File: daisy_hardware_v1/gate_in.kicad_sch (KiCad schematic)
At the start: 5 parts, among them J6 PJ398SM-12, Q1 MMBT3904

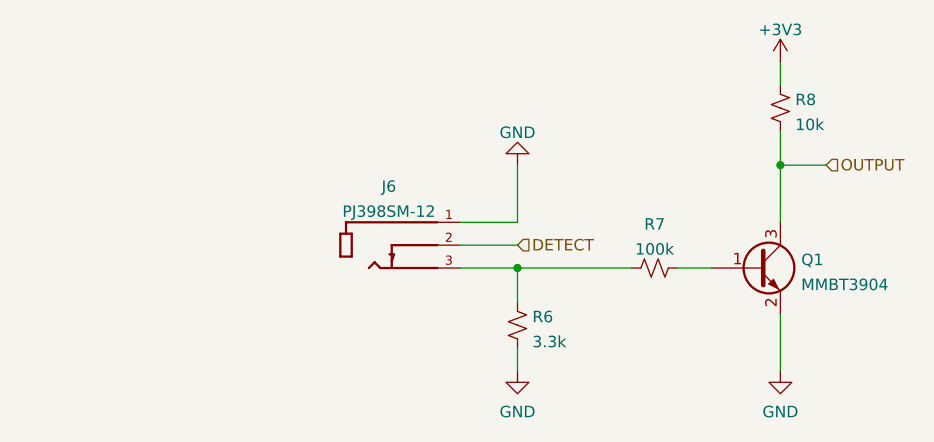
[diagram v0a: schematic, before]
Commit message: first pass of daisy schematic
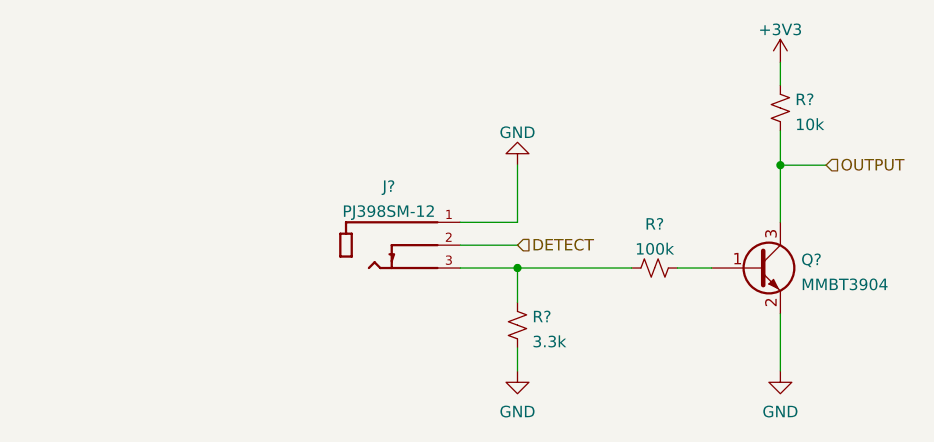
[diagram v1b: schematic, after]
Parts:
- renumbered J6 to J?, Q1 to Q?, R8 to R?, R7 to R?, R6 to R?
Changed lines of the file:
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@@
   (symbol (lib_id "Device:R_Small_US") (at 121.92 91.44 180)
     (in_bom yes) (on_board yes) (fields_autoplaced)
-    (property "Reference" "R8" (id 0) (at 123.571 90.5315 0)
+    (property "Reference" "R?" (id 0) (at 123.571 90.5315 0)
       (effects (font (size 1.27 1.27)) (justify right))
     )
@@
   (symbol (lib_id "power:GND") (at 121.92 120.65 0)
     (in_bom yes) (on_board yes) (fields_autoplaced)
-    (property "Reference" "#PWR0137" (id 0) (at 121.92 127 0)
+    (property "Reference" "#PWR?" (id 0) (at 121.92 127 0)
       (effects (font (size 1.27 1.27)) hide)
     )
@@
   (symbol (lib_id "power:GND") (at 92.71 120.65 0)
     (in_bom yes) (on_board yes) (fields_autoplaced)
-    (property "Reference" "#PWR0138" (id 0) (at 92.71 127 0)
+    (property "Reference" "#PWR?" (id 0) (at 92.71 127 0)
       (effects (font (size 1.27 1.27)) hide)
     )
@@
   (symbol (lib_id "PJ398SM-12:PJ398SM-12") (at 78.74 104.14 0)
     (in_bom yes) (on_board yes) (fields_autoplaced)
-    (property "Reference" "J6" (id 0) (at 78.4225 100.1735 0))
+    (property "Reference" "J?" (id 0) (at 78.4225 100.1735 0))
     (property "Value" "PJ398SM-12" (id 1) (at 78.4225 102.9486 0))
     (property "Footprint" "THONK_PJ398SM-12" (id 2) (at 78.74 104.14 0)
@@
   (symbol (lib_id "power:GND") (at 92.71 97.79 180)
     (in_bom yes) (on_board yes) (fields_autoplaced)
-    (property "Reference" "#PWR0136" (id 0) (at 92.71 91.44 0)
+    (property "Reference" "#PWR?" (id 0) (at 92.71 91.44 0)
       (effects (font (size 1.27 1.27)) hide)
     )
@@
   (symbol (lib_id "Device:R_Small_US") (at 107.95 109.22 90)
     (in_bom yes) (on_board yes) (fields_autoplaced)
-    (property "Reference" "R7" (id 0) (at 107.95 104.3645 90))
+    (property "Reference" "R?" (id 0) (at 107.95 104.3645 90))
     (property "Value" "100k" (id 1) (at 107.95 107.1396 90))
     (property "Footprint" "" (id 2) (at 107.95 109.22 0)
@@
   (symbol (lib_id "Transistor_BJT:MMBT3904") (at 119.38 109.22 0)
     (in_bom yes) (on_board yes) (fields_autoplaced)
-    (property "Reference" "Q1" (id 0) (at 124.2314 108.3115 0)
+    (property "Reference" "Q?" (id 0) (at 124.2314 108.3115 0)
       (effects (font (size 1.27 1.27)) (justify left))
     )
@@
   (symbol (lib_id "power:+3V3") (at 121.92 86.36 0)
     (in_bom yes) (on_board yes) (fields_autoplaced)
-    (property "Reference" "#PWR0139" (id 0) (at 121.92 90.17 0)
+    (property "Reference" "#PWR?" (id 0) (at 121.92 90.17 0)
       (effects (font (size 1.27 1.27)) hide)
     )
@@
   (symbol (lib_id "Device:R_Small_US") (at 92.71 115.57 0)
     (in_bom yes) (on_board yes) (fields_autoplaced)
-    (property "Reference" "R6" (id 0) (at 94.361 114.6615 0)
+    (property "Reference" "R?" (id 0) (at 94.361 114.6615 0)
       (effects (font (size 1.27 1.27)) (justify left))
     )

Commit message: Schematics coming along
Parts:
- J7: renamed from J?; footprint THONK_PJ398SM-12 -> Connector_Audio:Jack_3.5mm_QingPu_WQP-PJ398SM_Vertical_CircularHoles
- gave numbers to parts that had none: 4
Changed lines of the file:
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@@
   (symbol (lib_id "Device:R_Small_US") (at 121.92 91.44 180)
     (in_bom yes) (on_board yes) (fields_autoplaced)
-    (property "Reference" "R?" (id 0) (at 123.571 90.5315 0)
+    (property "Reference" "R11" (id 0) (at 123.571 90.5315 0)
       (effects (font (size 1.27 1.27)) (justify right))
     )
@@
   (symbol (lib_id "power:GND") (at 121.92 120.65 0)
     (in_bom yes) (on_board yes) (fields_autoplaced)
-    (property "Reference" "#PWR?" (id 0) (at 121.92 127 0)
+    (property "Reference" "#PWR0141" (id 0) (at 121.92 127 0)
       (effects (font (size 1.27 1.27)) hide)
     )
@@
   (symbol (lib_id "power:GND") (at 92.71 120.65 0)
     (in_bom yes) (on_board yes) (fields_autoplaced)
-    (property "Reference" "#PWR?" (id 0) (at 92.71 127 0)
+    (property "Reference" "#PWR0142" (id 0) (at 92.71 127 0)
       (effects (font (size 1.27 1.27)) hide)
     )
@@
   (symbol (lib_id "PJ398SM-12:PJ398SM-12") (at 78.74 104.14 0)
     (in_bom yes) (on_board yes) (fields_autoplaced)
-    (property "Reference" "J?" (id 0) (at 78.4225 100.1735 0))
+    (property "Reference" "J7" (id 0) (at 78.4225 100.1735 0))
     (property "Value" "PJ398SM-12" (id 1) (at 78.4225 102.9486 0))
-    (property "Footprint" "THONK_PJ398SM-12" (id 2) (at 78.74 104.14 0)
+    (property "Footprint" "Connector_Audio:Jack_3.5mm_QingPu_WQP-PJ398SM_Vertical_CircularHoles" (id 2) (at 78.74 104.14 0)
       (effects (font (size 1.27 1.27)) (justify left bottom) hide)
     )
@@
   (symbol (lib_id "power:GND") (at 92.71 97.79 180)
     (in_bom yes) (on_board yes) (fields_autoplaced)
-    (property "Reference" "#PWR?" (id 0) (at 92.71 91.44 0)
+    (property "Reference" "#PWR0140" (id 0) (at 92.71 91.44 0)
       (effects (font (size 1.27 1.27)) hide)
     )
@@
   (symbol (lib_id "Device:R_Small_US") (at 107.95 109.22 90)
     (in_bom yes) (on_board yes) (fields_autoplaced)
-    (property "Reference" "R?" (id 0) (at 107.95 104.3645 90))
+    (property "Reference" "R10" (id 0) (at 107.95 104.3645 90))
     (property "Value" "100k" (id 1) (at 107.95 107.1396 90))
     (property "Footprint" "" (id 2) (at 107.95 109.22 0)
@@
   (symbol (lib_id "Transistor_BJT:MMBT3904") (at 119.38 109.22 0)
     (in_bom yes) (on_board yes) (fields_autoplaced)
-    (property "Reference" "Q?" (id 0) (at 124.2314 108.3115 0)
+    (property "Reference" "Q2" (id 0) (at 124.2314 108.3115 0)
       (effects (font (size 1.27 1.27)) (justify left))
     )
@@
   (symbol (lib_id "power:+3V3") (at 121.92 86.36 0)
     (in_bom yes) (on_board yes) (fields_autoplaced)
-    (property "Reference" "#PWR?" (id 0) (at 121.92 90.17 0)
+    (property "Reference" "#PWR0143" (id 0) (at 121.92 90.17 0)
       (effects (font (size 1.27 1.27)) hide)
     )
@@
   (symbol (lib_id "Device:R_Small_US") (at 92.71 115.57 0)
     (in_bom yes) (on_board yes) (fields_autoplaced)
-    (property "Reference" "R?" (id 0) (at 94.361 114.6615 0)
+    (property "Reference" "R9" (id 0) (at 94.361 114.6615 0)
       (effects (font (size 1.27 1.27)) (justify left))
     )

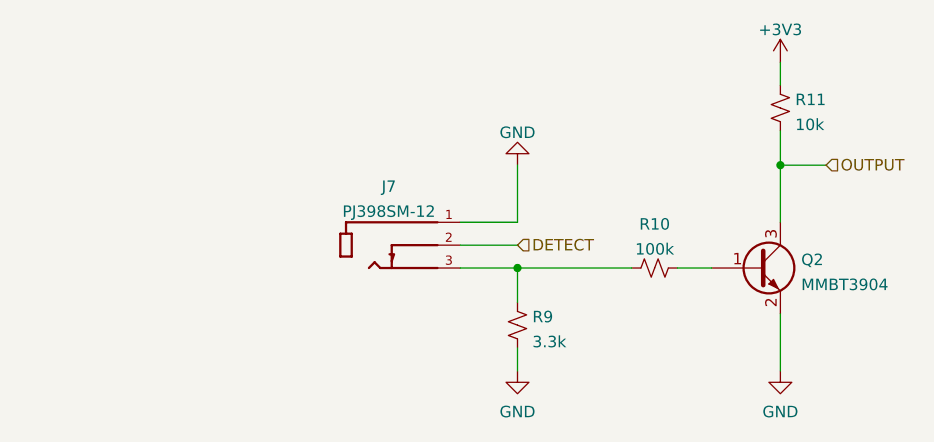
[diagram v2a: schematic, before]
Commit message: Update power + add start/end to schematics
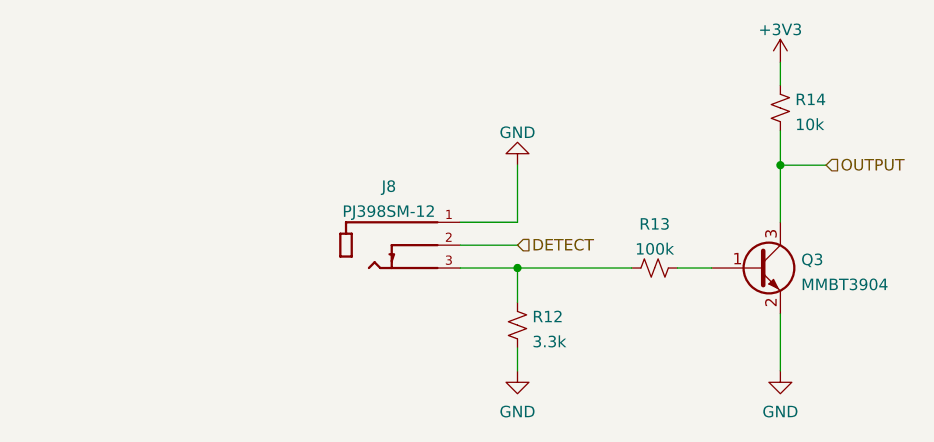
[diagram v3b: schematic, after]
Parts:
- J8: renamed from J7; footprint Connector_Audio:Jack_3.5mm_QingPu_WQP-PJ398SM_Vertical_CircularHoles -> lowstepper_internal_footprint_lib:THONK_PJ398SM-12
- renumbered Q2 to Q3, R9 to R12, R10 to R13, R11 to R14
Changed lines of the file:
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@@
   (symbol (lib_id "Device:R_Small_US") (at 121.92 91.44 180)
     (in_bom yes) (on_board yes) (fields_autoplaced)
-    (property "Reference" "R11" (id 0) (at 123.571 90.5315 0)
+    (property "Reference" "R14" (id 0) (at 123.571 90.5315 0)
       (effects (font (size 1.27 1.27)) (justify right))
     )
@@
   (symbol (lib_id "power:GND") (at 121.92 120.65 0)
     (in_bom yes) (on_board yes) (fields_autoplaced)
-    (property "Reference" "#PWR0141" (id 0) (at 121.92 127 0)
+    (property "Reference" "#PWR0157" (id 0) (at 121.92 127 0)
       (effects (font (size 1.27 1.27)) hide)
     )
@@
   (symbol (lib_id "power:GND") (at 92.71 120.65 0)
     (in_bom yes) (on_board yes) (fields_autoplaced)
-    (property "Reference" "#PWR0142" (id 0) (at 92.71 127 0)
+    (property "Reference" "#PWR0158" (id 0) (at 92.71 127 0)
       (effects (font (size 1.27 1.27)) hide)
     )
@@
   (symbol (lib_id "PJ398SM-12:PJ398SM-12") (at 78.74 104.14 0)
     (in_bom yes) (on_board yes) (fields_autoplaced)
-    (property "Reference" "J7" (id 0) (at 78.4225 100.1735 0))
+    (property "Reference" "J8" (id 0) (at 78.4225 100.1735 0))
     (property "Value" "PJ398SM-12" (id 1) (at 78.4225 102.9486 0))
-    (property "Footprint" "Connector_Audio:Jack_3.5mm_QingPu_WQP-PJ398SM_Vertical_CircularHoles" (id 2) (at 78.74 104.14 0)
+    (property "Footprint" "lowstepper_internal_footprint_lib:THONK_PJ398SM-12" (id 2) (at 78.74 104.14 0)
       (effects (font (size 1.27 1.27)) (justify left bottom) hide)
     )
@@
   (symbol (lib_id "power:GND") (at 92.71 97.79 180)
     (in_bom yes) (on_board yes) (fields_autoplaced)
-    (property "Reference" "#PWR0140" (id 0) (at 92.71 91.44 0)
+    (property "Reference" "#PWR0156" (id 0) (at 92.71 91.44 0)
       (effects (font (size 1.27 1.27)) hide)
     )
@@
   (symbol (lib_id "Device:R_Small_US") (at 107.95 109.22 90)
     (in_bom yes) (on_board yes) (fields_autoplaced)
-    (property "Reference" "R10" (id 0) (at 107.95 104.3645 90))
+    (property "Reference" "R13" (id 0) (at 107.95 104.3645 90))
     (property "Value" "100k" (id 1) (at 107.95 107.1396 90))
     (property "Footprint" "" (id 2) (at 107.95 109.22 0)
@@
   (symbol (lib_id "Transistor_BJT:MMBT3904") (at 119.38 109.22 0)
     (in_bom yes) (on_board yes) (fields_autoplaced)
-    (property "Reference" "Q2" (id 0) (at 124.2314 108.3115 0)
+    (property "Reference" "Q3" (id 0) (at 124.2314 108.3115 0)
       (effects (font (size 1.27 1.27)) (justify left))
     )
@@
   (symbol (lib_id "power:+3V3") (at 121.92 86.36 0)
     (in_bom yes) (on_board yes) (fields_autoplaced)
-    (property "Reference" "#PWR0143" (id 0) (at 121.92 90.17 0)
+    (property "Reference" "#PWR0159" (id 0) (at 121.92 90.17 0)
       (effects (font (size 1.27 1.27)) hide)
     )
@@
   (symbol (lib_id "Device:R_Small_US") (at 92.71 115.57 0)
     (in_bom yes) (on_board yes) (fields_autoplaced)
-    (property "Reference" "R9" (id 0) (at 94.361 114.6615 0)
+    (property "Reference" "R12" (id 0) (at 94.361 114.6615 0)
       (effects (font (size 1.27 1.27)) (justify left))
     )

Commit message: Start splitting up board
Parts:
- R10: renamed from R13; footprint (none) -> Resistor_SMD:R_0603_1608Metric
- R11: renamed from R14; footprint (none) -> Resistor_SMD:R_0603_1608Metric
- R9: renamed from R12; footprint (none) -> Resistor_SMD:R_0603_1608Metric
- renumbered J8 to J7, Q3 to Q2
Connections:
- net INPUT_BOTTOM: now reaches R10.1, R9.1
- net INPUT_BOTTOM: no longer J7.3
- new net INPUT_TOP: J7.3
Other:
- moved on the sheet: J7
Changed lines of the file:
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@@
     (stroke (width 0) (type default) (color 0 0 0 0))
   )
-  (wire (pts (xy 86.36 104.14) (xy 92.71 104.14))
+  (wire (pts (xy 52.07 104.14) (xy 92.71 104.14))
     (stroke (width 0) (type default) (color 0 0 0 0))
   )
   (wire (pts (xy 86.36 109.22) (xy 92.71 109.22))
+    (stroke (width 0) (type default) (color 0 0 0 0))
+  )
+  (wire (pts (xy 52.07 109.22) (xy 54.61 109.22))
     (stroke (width 0) (type default) (color 0 0 0 0))
   )
@@
     (stroke (width 0) (type default) (color 0 0 0 0))
   )
-  (wire (pts (xy 86.36 106.68) (xy 92.71 106.68))
+  (wire (pts (xy 52.07 106.68) (xy 92.71 106.68))
     (stroke (width 0) (type default) (color 0 0 0 0))
   )
   (wire (pts (xy 121.92 114.3) (xy 121.92 120.65))
     (stroke (width 0) (type default) (color 0 0 0 0))
+  )
+  (hierarchical_label "INPUT_BOTTOM" (shape input) (at 86.36 109.22 180)
+    (effects (font (size 1.27 1.27)) (justify right))
+  )
+  (hierarchical_label "INPUT_TOP" (shape input) (at 54.61 109.22 0)
+    (effects (font (size 1.27 1.27)) (justify left))
   )
   (hierarchical_label "DETECT" (shape input) (at 92.71 106.68 0)
@@
   (symbol (lib_id "Device:R_Small_US") (at 121.92 91.44 180)
     (in_bom yes) (on_board yes) (fields_autoplaced)
-    (property "Reference" "R14" (id 0) (at 123.571 90.5315 0)
+    (property "Reference" "R11" (id 0) (at 123.571 90.5315 0)
       (effects (font (size 1.27 1.27)) (justify right))
     )
@@
       (effects (font (size 1.27 1.27)) (justify right))
     )
-    (property "Footprint" "" (id 2) (at 121.92 91.44 0)
+    (property "Footprint" "Resistor_SMD:R_0603_1608Metric" (id 2) (at 121.92 91.44 0)
       (effects (font (size 1.27 1.27)) hide)
     )
@@
   (symbol (lib_id "power:GND") (at 121.92 120.65 0)
     (in_bom yes) (on_board yes) (fields_autoplaced)
-    (property "Reference" "#PWR0157" (id 0) (at 121.92 127 0)
+    (property "Reference" "#PWR0141" (id 0) (at 121.92 127 0)
       (effects (font (size 1.27 1.27)) hide)
     )
@@
   (symbol (lib_id "power:GND") (at 92.71 120.65 0)
     (in_bom yes) (on_board yes) (fields_autoplaced)
-    (property "Reference" "#PWR0158" (id 0) (at 92.71 127 0)
+    (property "Reference" "#PWR0142" (id 0) (at 92.71 127 0)
       (effects (font (size 1.27 1.27)) hide)
     )
@@
     (pin "1")
   )
-  (symbol (lib_id "PJ398SM-12:PJ398SM-12") (at 78.74 104.14 0)
+  (symbol (lib_id "PJ398SM-12:PJ398SM-12") (at 44.45 104.14 0)
     (in_bom yes) (on_board yes) (fields_autoplaced)
-    (property "Reference" "J8" (id 0) (at 78.4225 100.1735 0))
-    (property "Value" "PJ398SM-12" (id 1) (at 78.4225 102.9486 0))
-    (property "Footprint" "lowstepper_internal_footprint_lib:THONK_PJ398SM-12" (id 2) (at 78.74 104.14 0)
+    (property "Reference" "J7" (id 0) (at 44.1325 100.1735 0))
+    (property "Value" "PJ398SM-12" (id 1) (at 44.1325 102.9486 0))
+    (property "Footprint" "lowstepper_internal_footprint_lib:THONK_PJ398SM-12" (id 2) (at 44.45 104.14 0)
       (effects (font (size 1.27 1.27)) (justify left bottom) hide)
     )
-    (property "Datasheet" "" (id 3) (at 78.74 104.14 0)
+    (property "Datasheet" "" (id 3) (at 44.45 104.14 0)
       (effects (font (size 1.27 1.27)) (justify left bottom) hide)
     )
-    (property "MAXIMUM_PACKAGE_HEIGHT" "14.5 mm" (id 4) (at 78.74 104.14 0)
+    (property "MAXIMUM_PACKAGE_HEIGHT" "14.5 mm" (id 4) (at 44.45 104.14 0)
       (effects (font (size 1.27 1.27)) (justify left bottom) hide)
     )
-    (property "MANUFACTURER" "Thonk" (id 5) (at 78.74 104.14 0)
+    (property "MANUFACTURER" "Thonk" (id 5) (at 44.45 104.14 0)
       (effects (font (size 1.27 1.27)) (justify left bottom) hide)
     )
-    (property "PARTREV" "1" (id 6) (at 78.74 104.14 0)
+    (property "PARTREV" "1" (id 6) (at 44.45 104.14 0)
       (effects (font (size 1.27 1.27)) (justify left bottom) hide)
     )
-    (property "STANDARD" "Manufacturer Recommendations" (id 7) (at 78.74 104.14 0)
+    (property "STANDARD" "Manufacturer Recommendations" (id 7) (at 44.45 104.14 0)
       (effects (font (size 1.27 1.27)) (justify left bottom) hide)
     )
@@
   (symbol (lib_id "power:GND") (at 92.71 97.79 180)
     (in_bom yes) (on_board yes) (fields_autoplaced)
-    (property "Reference" "#PWR0156" (id 0) (at 92.71 91.44 0)
+    (property "Reference" "#PWR0140" (id 0) (at 92.71 91.44 0)
       (effects (font (size 1.27 1.27)) hide)
     )
@@
   (symbol (lib_id "Device:R_Small_US") (at 107.95 109.22 90)
     (in_bom yes) (on_board yes) (fields_autoplaced)
-    (property "Reference" "R13" (id 0) (at 107.95 104.3645 90))
+    (property "Reference" "R10" (id 0) (at 107.95 104.3645 90))
     (property "Value" "100k" (id 1) (at 107.95 107.1396 90))
-    (property "Footprint" "" (id 2) (at 107.95 109.22 0)
+    (property "Footprint" "Resistor_SMD:R_0603_1608Metric" (id 2) (at 107.95 109.22 0)
       (effects (font (size 1.27 1.27)) hide)
     )
@@
   (symbol (lib_id "Transistor_BJT:MMBT3904") (at 119.38 109.22 0)
     (in_bom yes) (on_board yes) (fields_autoplaced)
-    (property "Reference" "Q3" (id 0) (at 124.2314 108.3115 0)
+    (property "Reference" "Q2" (id 0) (at 124.2314 108.3115 0)
       (effects (font (size 1.27 1.27)) (justify left))
     )
@@
   (symbol (lib_id "power:+3V3") (at 121.92 86.36 0)
     (in_bom yes) (on_board yes) (fields_autoplaced)
-    (property "Reference" "#PWR0159" (id 0) (at 121.92 90.17 0)
+    (property "Reference" "#PWR0143" (id 0) (at 121.92 90.17 0)
       (effects (font (size 1.27 1.27)) hide)
     )
@@
   (symbol (lib_id "Device:R_Small_US") (at 92.71 115.57 0)
     (in_bom yes) (on_board yes) (fields_autoplaced)
-    (property "Reference" "R12" (id 0) (at 94.361 114.6615 0)
+    (property "Reference" "R9" (id 0) (at 94.361 114.6615 0)
       (effects (font (size 1.27 1.27)) (justify left))
     )
@@
       (effects (font (size 1.27 1.27)) (justify left))
     )
-    (property "Footprint" "" (id 2) (at 92.71 115.57 0)
+    (property "Footprint" "Resistor_SMD:R_0603_1608Metric" (id 2) (at 92.71 115.57 0)
       (effects (font (size 1.27 1.27)) hide)
     )

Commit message: Almost done PCB
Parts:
- renumbered J7 to J11, Q2 to Q6, R9 to R21, R10 to R22, R11 to R23
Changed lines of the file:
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@@
   (symbol (lib_id "Device:R_Small_US") (at 121.92 91.44 180)
     (in_bom yes) (on_board yes) (fields_autoplaced)
-    (property "Reference" "R11" (id 0) (at 123.571 90.5315 0)
+    (property "Reference" "R23" (id 0) (at 123.571 90.5315 0)
       (effects (font (size 1.27 1.27)) (justify right))
     )
@@
   (symbol (lib_id "power:GND") (at 121.92 120.65 0)
     (in_bom yes) (on_board yes) (fields_autoplaced)
-    (property "Reference" "#PWR0141" (id 0) (at 121.92 127 0)
+    (property "Reference" "#PWR0157" (id 0) (at 121.92 127 0)
       (effects (font (size 1.27 1.27)) hide)
     )
@@
   (symbol (lib_id "power:GND") (at 92.71 120.65 0)
     (in_bom yes) (on_board yes) (fields_autoplaced)
-    (property "Reference" "#PWR0142" (id 0) (at 92.71 127 0)
+    (property "Reference" "#PWR0158" (id 0) (at 92.71 127 0)
       (effects (font (size 1.27 1.27)) hide)
     )
@@
   (symbol (lib_id "PJ398SM-12:PJ398SM-12") (at 44.45 104.14 0)
     (in_bom yes) (on_board yes) (fields_autoplaced)
-    (property "Reference" "J7" (id 0) (at 44.1325 100.1735 0))
+    (property "Reference" "J11" (id 0) (at 44.1325 100.1735 0))
     (property "Value" "PJ398SM-12" (id 1) (at 44.1325 102.9486 0))
     (property "Footprint" "lowstepper_internal_footprint_lib:THONK_PJ398SM-12" (id 2) (at 44.45 104.14 0)
@@
   (symbol (lib_id "power:GND") (at 92.71 97.79 180)
     (in_bom yes) (on_board yes) (fields_autoplaced)
-    (property "Reference" "#PWR0140" (id 0) (at 92.71 91.44 0)
+    (property "Reference" "#PWR0156" (id 0) (at 92.71 91.44 0)
       (effects (font (size 1.27 1.27)) hide)
     )
@@
   (symbol (lib_id "Device:R_Small_US") (at 107.95 109.22 90)
     (in_bom yes) (on_board yes) (fields_autoplaced)
-    (property "Reference" "R10" (id 0) (at 107.95 104.3645 90))
+    (property "Reference" "R22" (id 0) (at 107.95 104.3645 90))
     (property "Value" "100k" (id 1) (at 107.95 107.1396 90))
     (property "Footprint" "Resistor_SMD:R_0603_1608Metric" (id 2) (at 107.95 109.22 0)
@@
   (symbol (lib_id "Transistor_BJT:MMBT3904") (at 119.38 109.22 0)
     (in_bom yes) (on_board yes) (fields_autoplaced)
-    (property "Reference" "Q2" (id 0) (at 124.2314 108.3115 0)
+    (property "Reference" "Q6" (id 0) (at 124.2314 108.3115 0)
       (effects (font (size 1.27 1.27)) (justify left))
     )
@@
   (symbol (lib_id "power:+3V3") (at 121.92 86.36 0)
     (in_bom yes) (on_board yes) (fields_autoplaced)
-    (property "Reference" "#PWR0143" (id 0) (at 121.92 90.17 0)
+    (property "Reference" "#PWR0159" (id 0) (at 121.92 90.17 0)
       (effects (font (size 1.27 1.27)) hide)
     )
@@
   (symbol (lib_id "Device:R_Small_US") (at 92.71 115.57 0)
     (in_bom yes) (on_board yes) (fields_autoplaced)
-    (property "Reference" "R9" (id 0) (at 94.361 114.6615 0)
+    (property "Reference" "R21" (id 0) (at 94.361 114.6615 0)
       (effects (font (size 1.27 1.27)) (justify left))
     )
